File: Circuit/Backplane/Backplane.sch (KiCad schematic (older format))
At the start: 59 parts

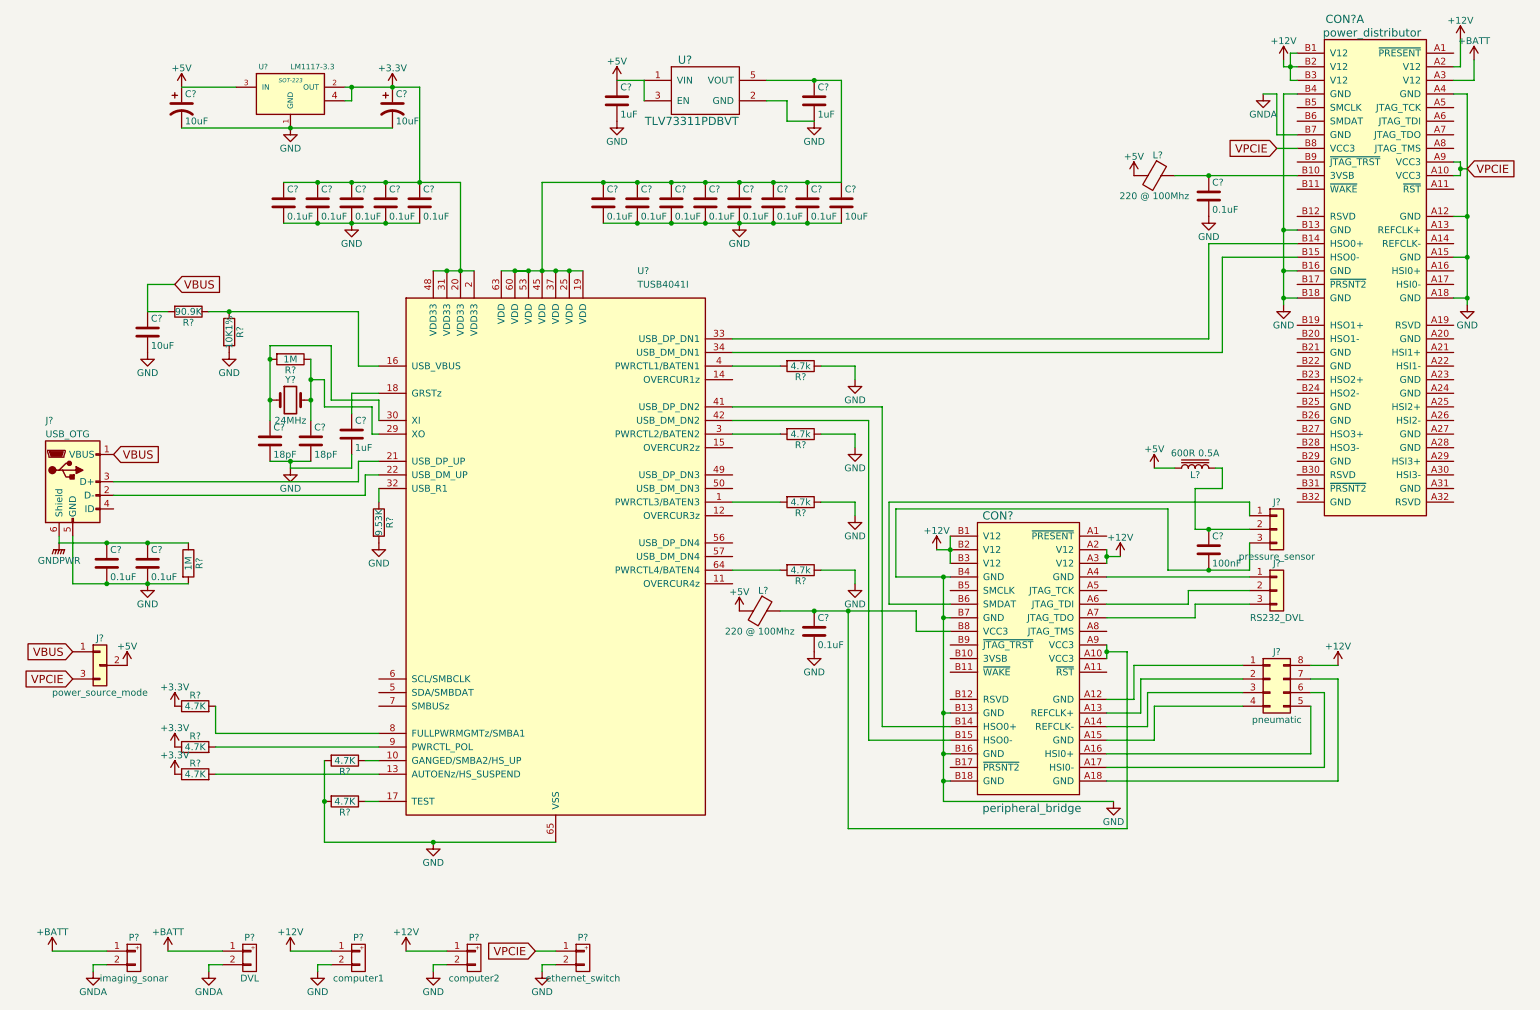
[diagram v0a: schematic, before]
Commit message: add 2 led on VBUS and VPCIe wire
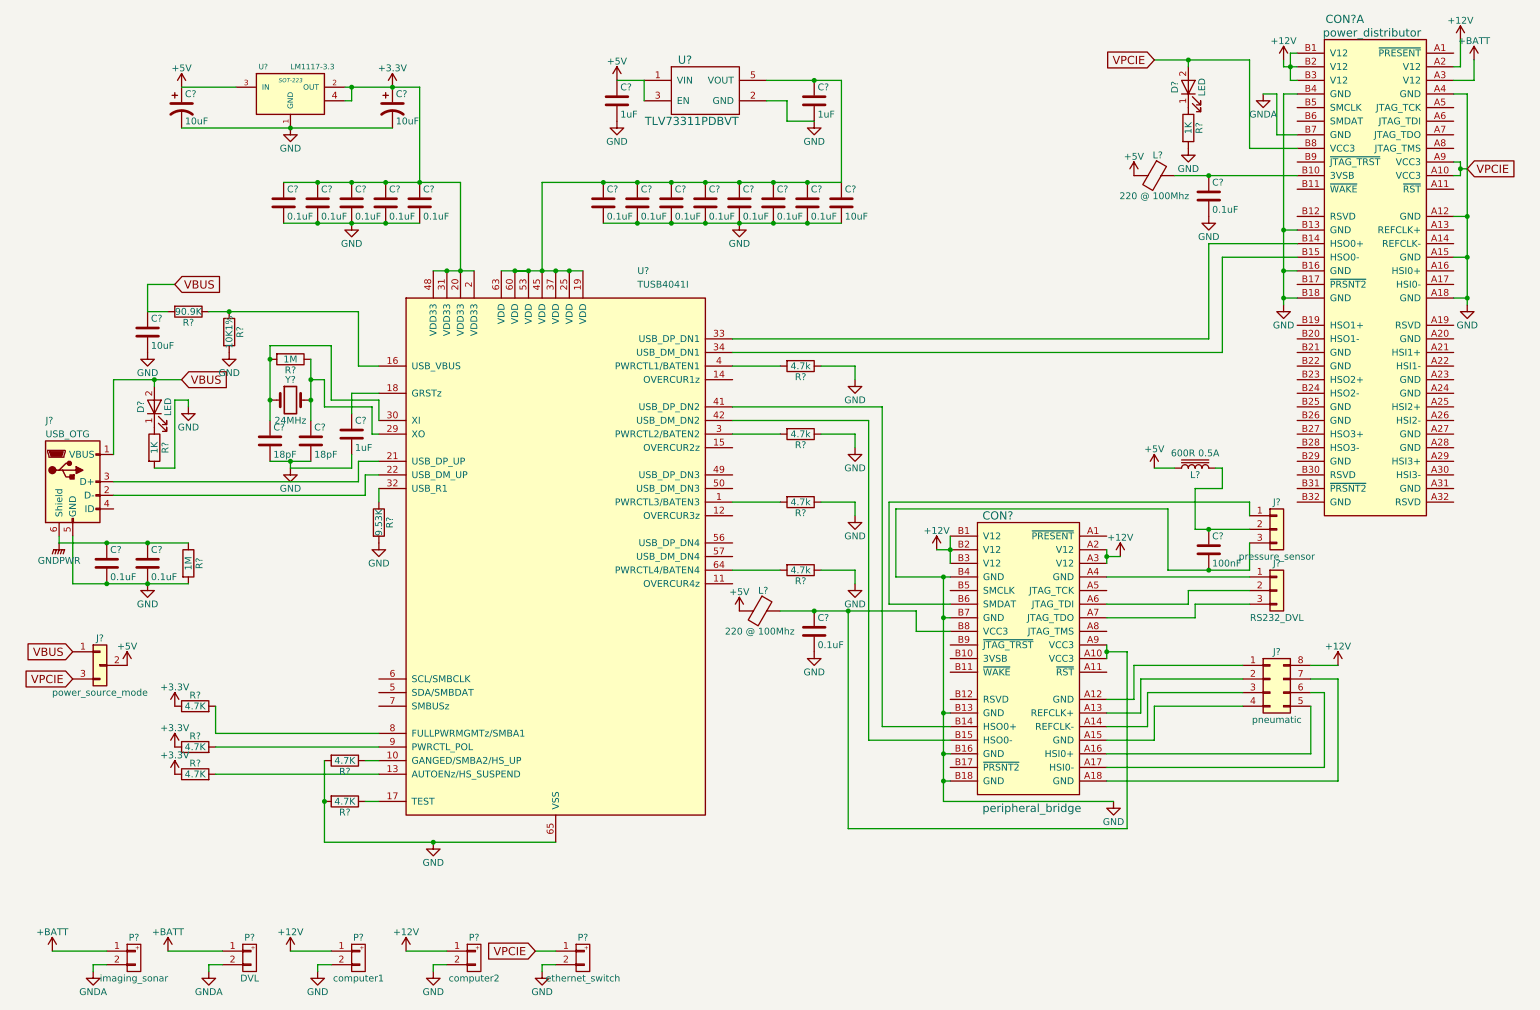
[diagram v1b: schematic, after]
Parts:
- added D? (x2): LED, symbol LED
- added R? (x2): 1K, symbol R
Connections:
- net GND: now also D?.2 (A), R?.2, R?.2
- net VBUS: now also D?.2 (A)
- new net: D?.1 (K), R?.1 (x2)
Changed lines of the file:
@@
 	1    0    0    -1
 $EndComp
-Text GLabel 1150 3700 2    60   Input ~ 0
+Text GLabel 1650 3150 2    60   Input ~ 0
 VBUS
 $Comp
@@
 	1    0    0    -1
 $EndComp
-Text GLabel 9700 1450 0    60   Input ~ 0
+Text GLabel 8800 800  0    60   Input ~ 0
 VPCIE
 Text GLabel 11100 1600 2    60   Input ~ 0
@@
 	0    -1   -1   0
 $EndComp
+$Comp
+L +12V #PWR?
+U 1 1 5A696562
+P 10150 5250
+F 0 "#PWR?" H 10150 5100 50  0001 C CNN
+F 1 "+12V" H 10150 5390 50  0000 C CNN
+F 2 "" H 10150 5250 50  0001 C CNN
+F 3 "" H 10150 5250 50  0001 C CNN
+	1    10150 5250
+	1    0    0    -1
+$EndComp
 Wire Wire Line
 	6800 5700 7300 5700
@@
 	9700 1050 9600 1050
 Wire Wire Line
-	9850 1450 9700 1450
+	9500 1450 9850 1450
 Wire Wire Line
 	9850 2150 9200 2150
@@
 Wire Wire Line
 	9950 5250 10150 5250
-$Comp
-L +12V #PWR?
-U 1 1 5A696562
-P 10150 5250
-F 0 "#PWR?" H 10150 5100 50  0001 C CNN
-F 1 "+12V" H 10150 5390 50  0000 C CNN
-F 2 "" H 10150 5250 50  0001 C CNN
-F 3 "" H 10150 5250 50  0001 C CNN
-	1    10150 5250
-	1    0    0    -1
-$EndComp
+Wire Wire Line
+	8800 800  9500 800
+Wire Wire Line
+	9500 800  9500 1450
+Wire Wire Line
+	9050 800  9050 850
+Connection ~ 9050 800
+$Comp
+L LED D?
+U 1 1 5A628BE7
+P 9050 1000
+F 0 "D?" H 9050 1100 50  0000 C CNN
+F 1 "LED" H 9050 900 50  0000 C CNN
+F 2 "" H 9050 1000 50  0001 C CNN
+F 3 "" H 9050 1000 50  0001 C CNN
+	1    9050 1000
+	0    -1   -1   0
+$EndComp
+$Comp
+L R R?
+U 1 1 5A628E18
+P 9050 1300
+F 0 "R?" V 9130 1300 50  0000 C CNN
+F 1 "1K" V 9050 1300 50  0000 C CNN
+F 2 "" V 8980 1300 50  0001 C CNN
+F 3 "" H 9050 1300 50  0001 C CNN
+	1    9050 1300
+	1    0    0    -1
+$EndComp
+$Comp
+L GND #PWR?
+U 1 1 5A628F8E
+P 9050 1450
+F 0 "#PWR?" H 9050 1200 50  0001 C CNN
+F 1 "GND" H 9050 1300 50  0000 C CNN
+F 2 "" H 9050 1450 50  0001 C CNN
+F 3 "" H 9050 1450 50  0001 C CNN
+	1    9050 1450
+	1    0    0    -1
+$EndComp
+Wire Wire Line
+	1150 3700 1150 3150
+Wire Wire Line
+	1150 3150 1650 3150
+Wire Wire Line
+	1450 3150 1450 3200
+Connection ~ 1450 3150
+$Comp
+L LED D?
+U 1 1 5A62976E
+P 1450 3350
+F 0 "D?" H 1450 3450 50  0000 C CNN
+F 1 "LED" H 1450 3250 50  0000 C CNN
+F 2 "" H 1450 3350 50  0001 C CNN
+F 3 "" H 1450 3350 50  0001 C CNN
+	1    1450 3350
+	0    -1   -1   0
+$EndComp
+$Comp
+L R R?
+U 1 1 5A629817
+P 1450 3650
+F 0 "R?" V 1530 3650 50  0000 C CNN
+F 1 "1K" V 1450 3650 50  0000 C CNN
+F 2 "" V 1380 3650 50  0001 C CNN
+F 3 "" H 1450 3650 50  0001 C CNN
+	1    1450 3650
+	1    0    0    -1
+$EndComp
+Wire Wire Line
+	1450 3800 1600 3800
+Wire Wire Line
+	1600 3800 1600 3300
+Wire Wire Line
+	1600 3300 1700 3300
+Wire Wire Line
+	1700 3300 1700 3350
+$Comp
+L GND #PWR?
+U 1 1 5A629A10
+P 1700 3350
+F 0 "#PWR?" H 1700 3100 50  0001 C CNN
+F 1 "GND" H 1700 3200 50  0000 C CNN
+F 2 "" H 1700 3350 50  0001 C CNN
+F 3 "" H 1700 3350 50  0001 C CNN
+	1    1700 3350
+	1    0    0    -1
+$EndComp

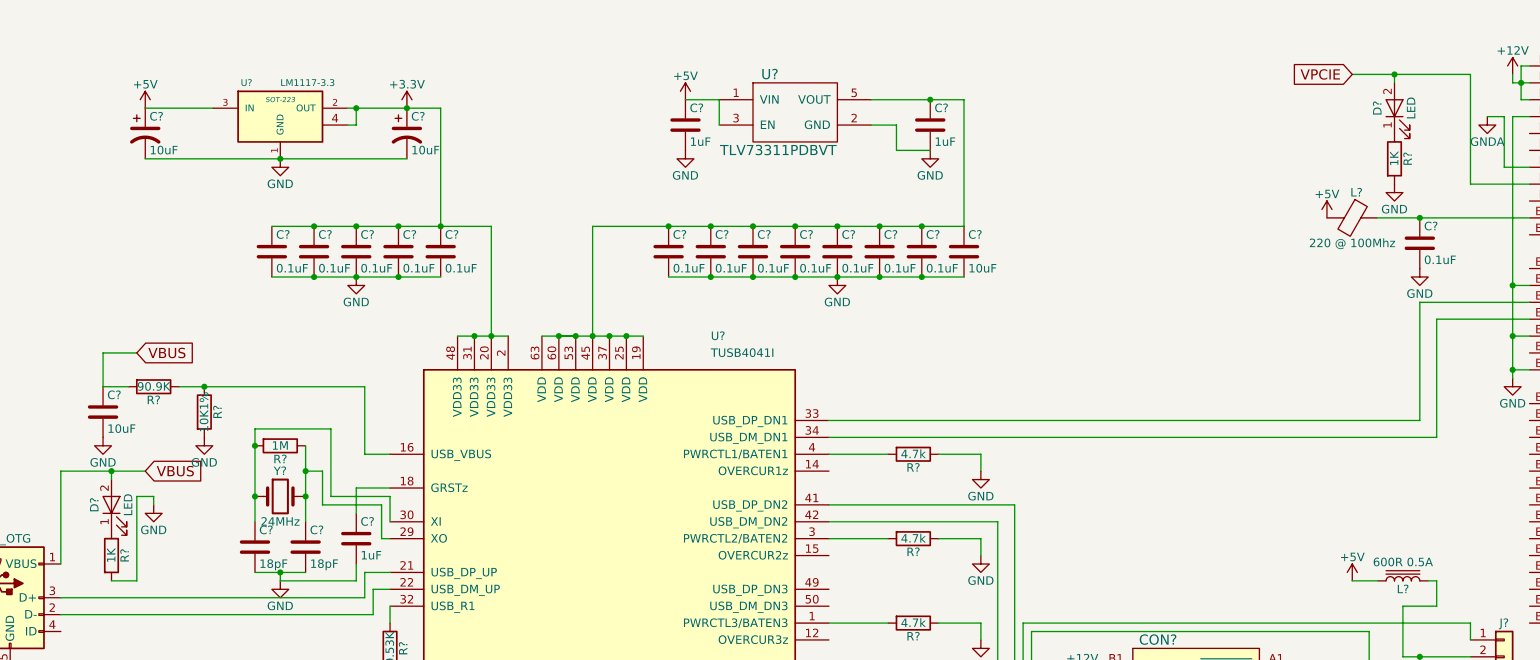
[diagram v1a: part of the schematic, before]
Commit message: led renamed
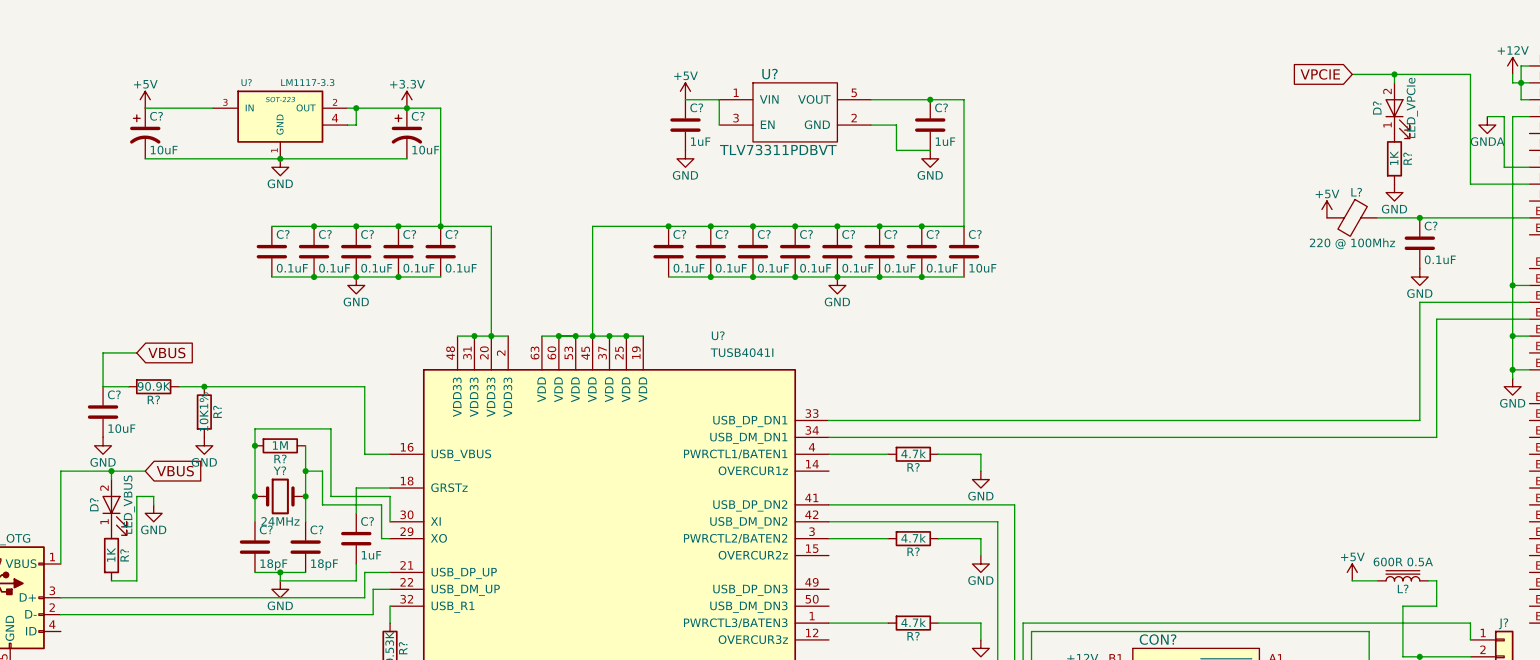
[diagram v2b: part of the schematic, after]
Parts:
- D?: value LED -> LED_VPCIe
- D?: value LED -> LED_VBUS
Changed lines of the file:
@@
 P 9050 1000
 F 0 "D?" H 9050 1100 50  0000 C CNN
-F 1 "LED" H 9050 900 50  0000 C CNN
+F 1 "LED_VPCIe" H 9050 900 50  0000 C CNN
 F 2 "" H 9050 1000 50  0001 C CNN
 F 3 "" H 9050 1000 50  0001 C CNN
@@
 P 1450 3350
 F 0 "D?" H 1450 3450 50  0000 C CNN
-F 1 "LED" H 1450 3250 50  0000 C CNN
+F 1 "LED_VBUS" H 1450 3250 50  0000 C CNN
 F 2 "" H 1450 3350 50  0001 C CNN
 F 3 "" H 1450 3350 50  0001 C CNN
